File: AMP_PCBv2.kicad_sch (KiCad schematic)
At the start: 2 parts, among them U1 Teensy4.0, U2 Logo

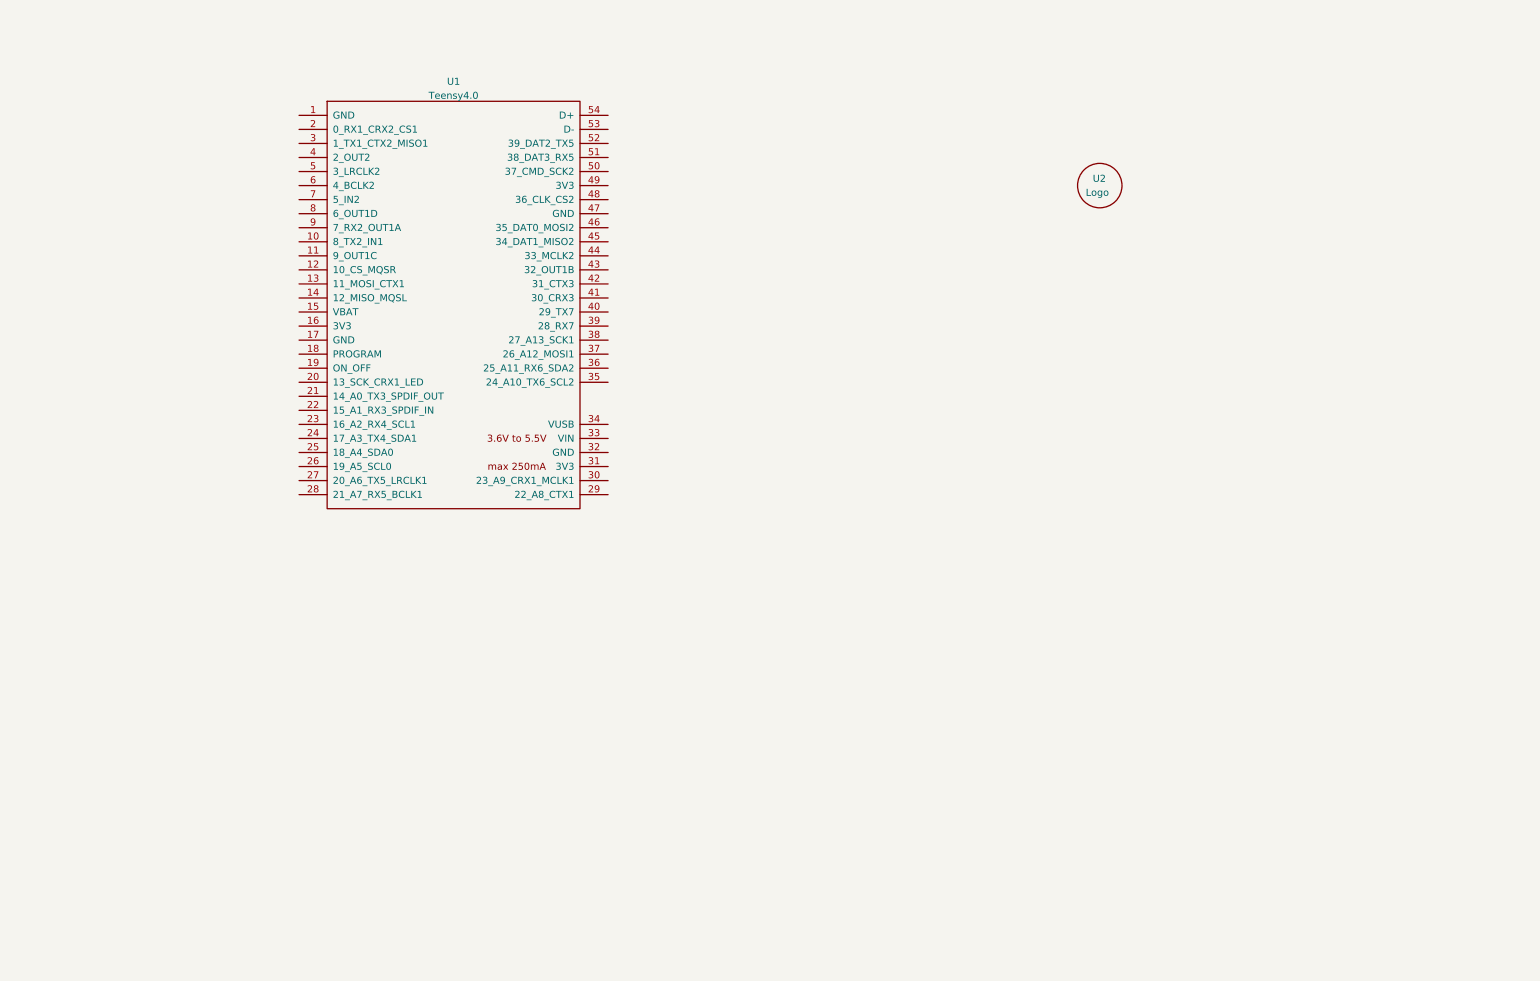
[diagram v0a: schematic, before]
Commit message: added bare bones schematic
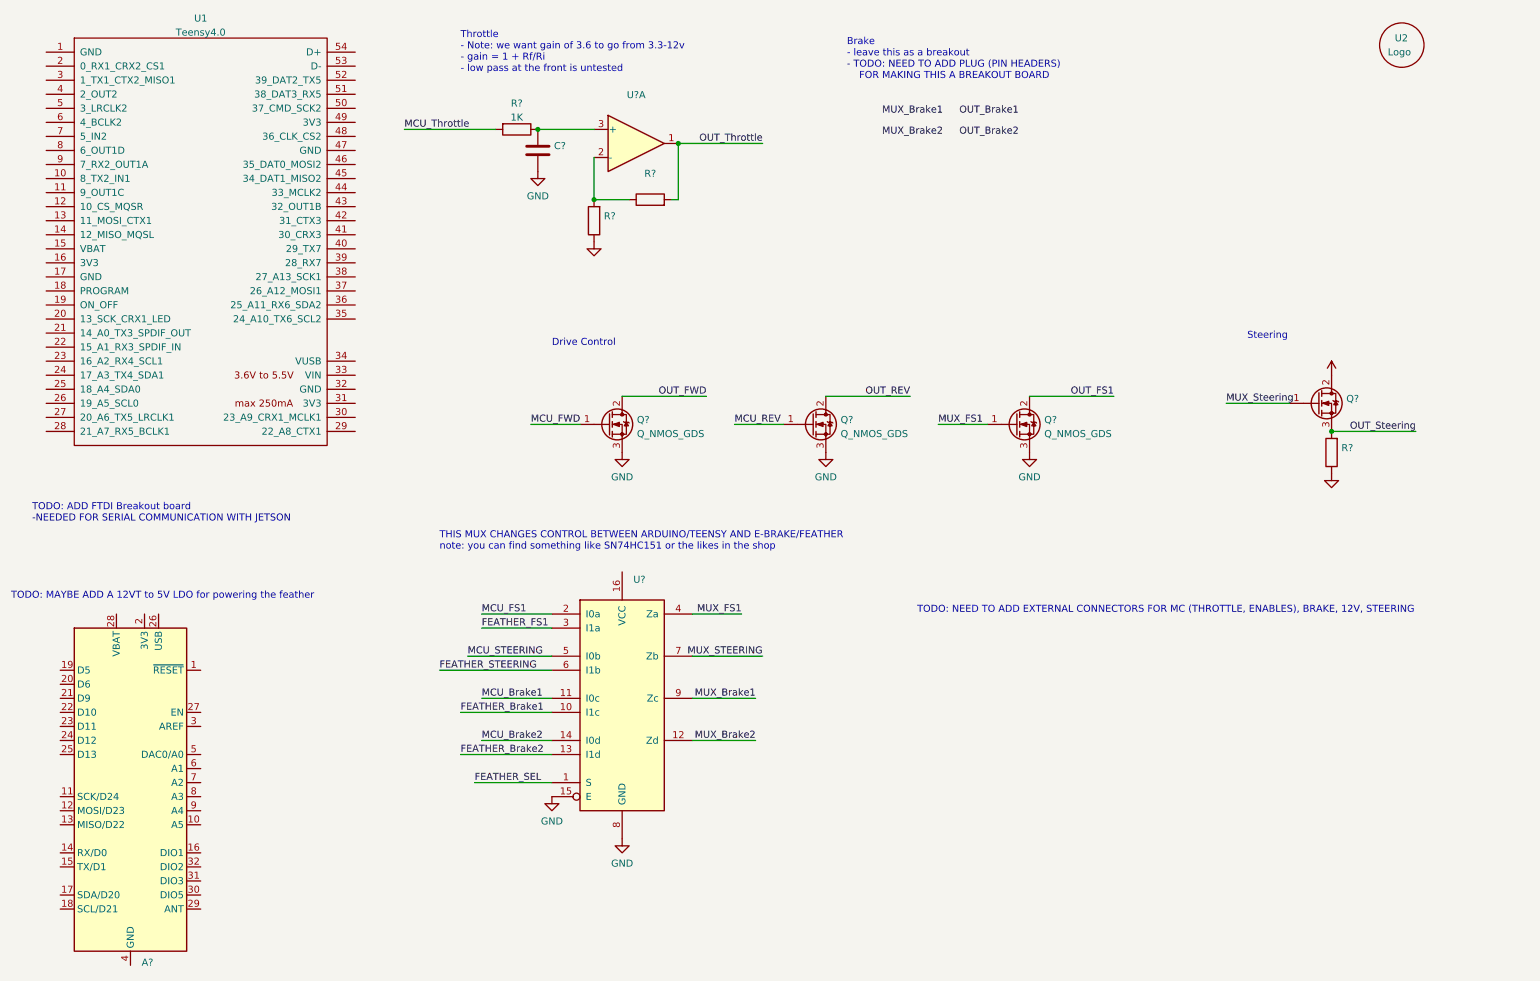
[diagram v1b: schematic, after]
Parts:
- added A?: (no value), symbol MCU_Module:Adafruit_Feather_M0_RFM9x_LoRa_Radio
- added C?: (no value), symbol Device:C
- added Q? (x3): Q_NMOS_GDS, symbol Device:Q_NMOS_GDS
- added Q?: (no value), symbol Device:Q_NMOS_GDS
- added R? (x3): (no value), symbol Device:R
- added R?: 1K, Resistor_THT:R_Axial_DIN0207_L6.3mm_D2.5mm_P10.16mm_Horizontal, symbol Device:R
- added U?: (no value), symbol Amplifier_Operational:TL084
- added U?: (no value), symbol 74xx:74LS157
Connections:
- new net: R?.1, R?.2, U?.2 (-)
- new net: C?.1, R?.1, U?.3 (+)
- new net +12V: Q?.2 (D)
- new net FEATHER_Brake1: U?.10 (I1c)
- new net FEATHER_Brake2: U?.13 (I1d)
- new net FEATHER_FS1: U?.3 (I1a)
- new net FEATHER_SEL: U?.1 (S)
- new net FEATHER_STEERING: U?.6 (I1b)
- new net GND: C?.2, Q?.3 (S), Q?.3 (S), Q?.3 (S), R?.1, R?.1, U?.15 (E), U?.8 (GND)
- new net MCU_Brake1: U?.11 (I0c)
- new net MCU_Brake2: U?.14 (I0d)
- new net MCU_FS1: U?.2 (I0a)
- new net MCU_FWD: Q?.1 (G)
- new net MCU_REV: Q?.1 (G)
- new net MCU_STEERING: U?.5 (I0b)
- new net MCU_Throttle: R?.2
- new net MUX_Brake1: U?.9 (Zc)
- new net MUX_Brake2: U?.12 (Zd)
- new net MUX_FS1: Q?.1 (G), U?.4 (Za)
- new net MUX_STEERING: U?.7 (Zb)
- new net MUX_Steering: Q?.1 (G)
- new net OUT_FS1: Q?.2 (D)
- new net OUT_FWD: Q?.2 (D)
- new net OUT_REV: Q?.2 (D)
- new net OUT_Steering: Q?.3 (S), R?.2
- new net OUT_Throttle: R?.2, U?.1
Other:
- note added: "Brake - leave this as a breakout - TODO: NEED TO ADD PLUG (PIN HEADERS) FOR MAKING THIS A BREAKOUT BOARD"
- note added: "Drive Control"
- note added: "Steering"
- note added: "THIS MUX CHANGES CONTROL BETWEEN ARDUINO/TEENSY AND E-BRAKE/FEATHER note: you can find something like SN74HC151 or the likes in the shop"
- note added: "TODO: ADD FTDI Breakout board -NEEDED FOR SERIAL COMMUNICATION WITH JETSON"
- note added: "TODO: MAYBE ADD A 12VT to 5V LDO for powering the feather"
- note added: "TODO: NEED TO ADD EXTERNAL CONNECTORS FOR MC (THROTTLE, ENABLES), BRAKE, 12V, STEERING"
- note added: "Throttle - Note: we want gain of 3.6 to go from 3.3-12v - gain = 1 + Rf/Ri - low pass at the front is untested"
- moved on the sheet: U1, U2

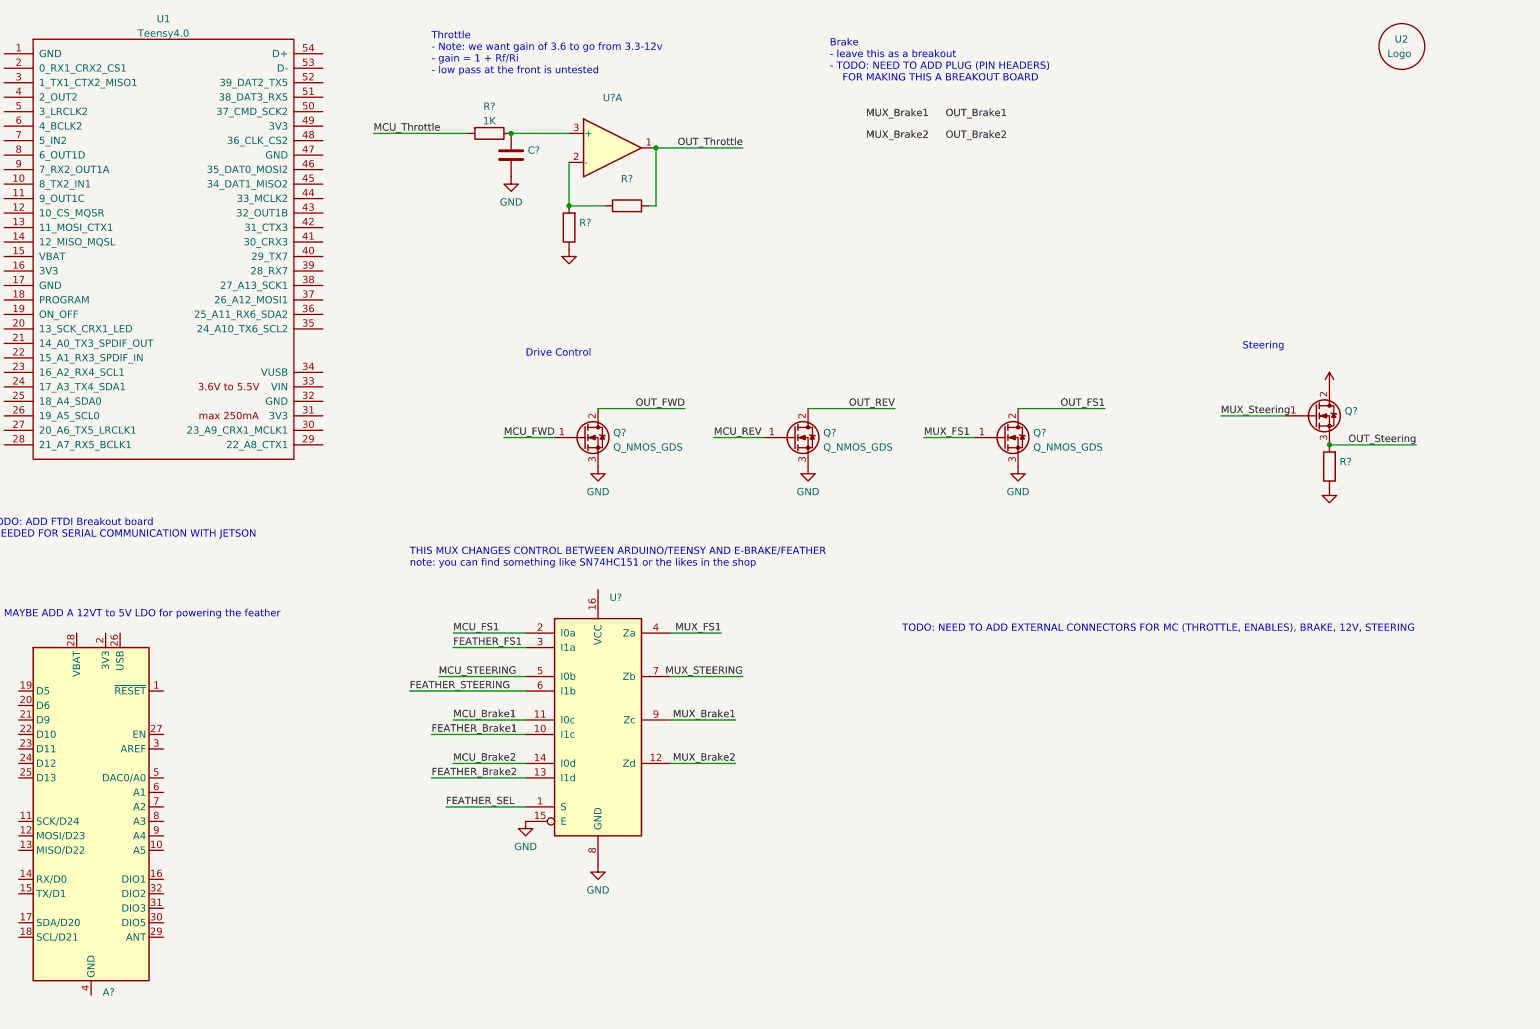
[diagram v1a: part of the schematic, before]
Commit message: Add MOSFET gate resistors, other misc cleanup
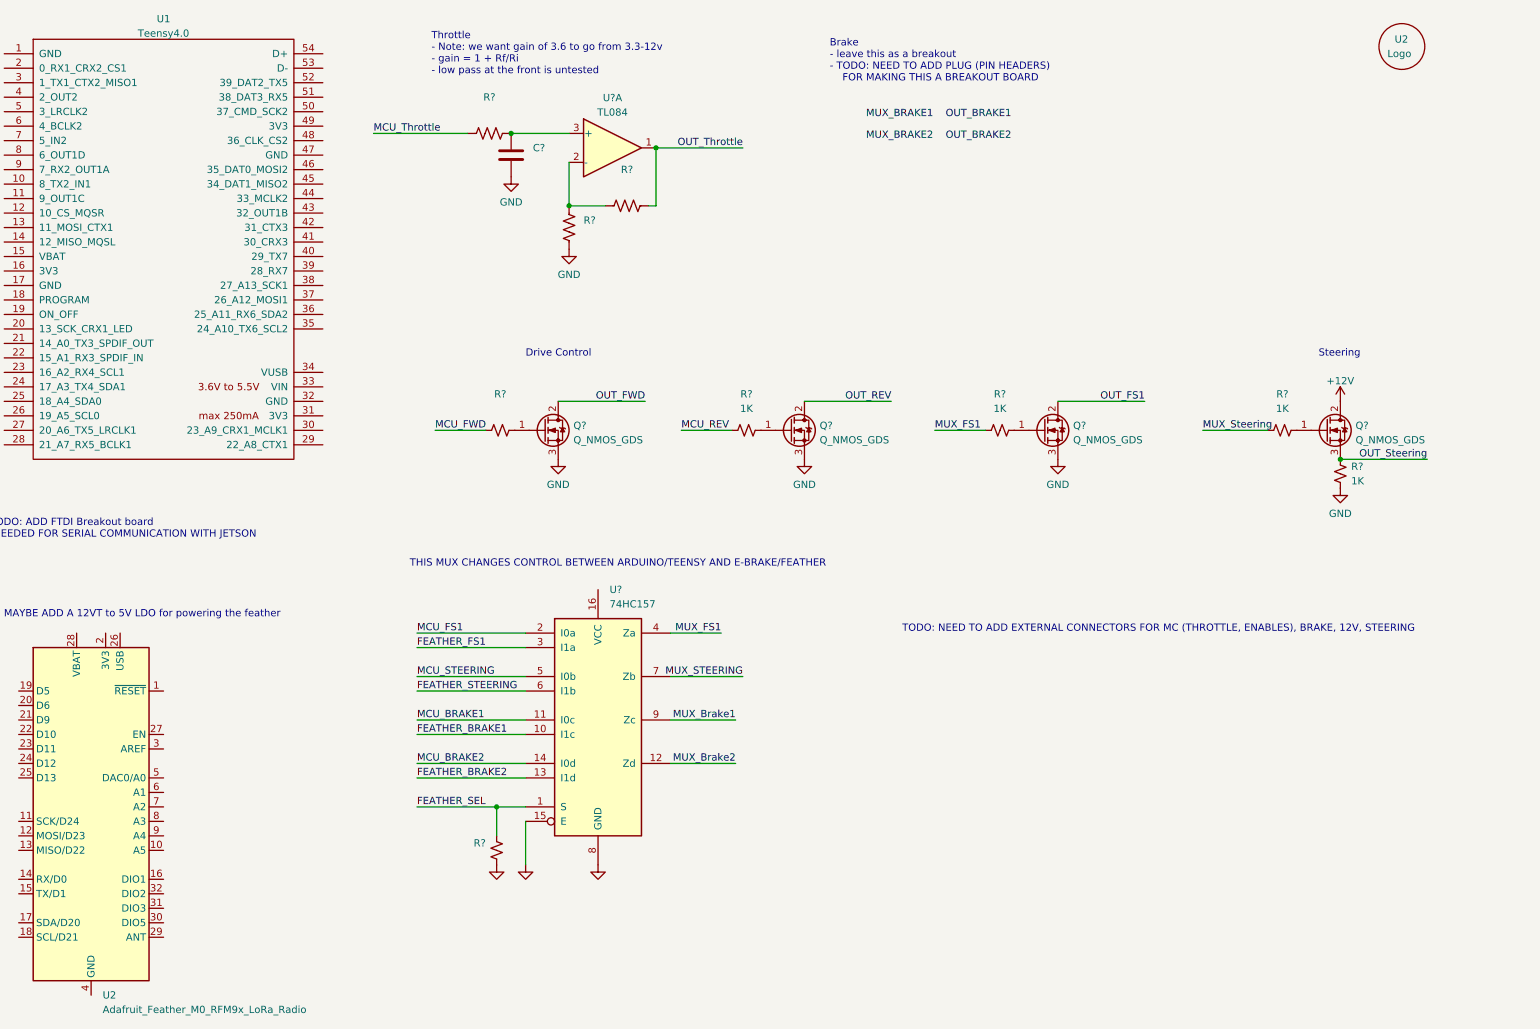
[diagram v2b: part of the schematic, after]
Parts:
- removed R? (x3): (no value), symbol Device:R
- removed R?: 1K, Resistor_THT:R_Axial_DIN0207_L6.3mm_D2.5mm_P10.16mm_Horizontal, symbol Device:R
- added R? (x2): (no value), symbol Device:R_Small_US
- added R? (x4): 1K, symbol Device:R_Small_US
- added R? (x3): (no value), symbol Device:R_US
- Q?: value (none) -> Q_NMOS_GDS
- U2: renamed from A?; value (none) -> Adafruit_Feather_M0_RFM9x_LoRa_Radio; footprint (none) -> Module:Adafruit_Feather_M0_RFM
- U?: value (none) -> TL084; footprint (none) -> Package_DIP:DIP-14_W7.62mm
- U?: value (none) -> 74HC157
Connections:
- net FEATHER_SEL: now also R?.1
- net GND: now also R?.1, R?.2, R?.2
- net MCU_FWD: now also R?.1; no longer Q?.1 (G)
- net MCU_REV: now also R?.1; no longer Q?.1 (G)
- net MCU_Throttle: now also R?.1
- net MUX_FS1: now also R?.1; no longer Q?.1 (G)
- net MUX_Steering: now also R?.1; no longer Q?.1 (G)
- net OUT_Steering: now also R?.2
- net OUT_Throttle: now also R?.2
- net at U?.2 (-): now also R?.1, R?.1
- net at C?.1, U?.3 (+): now also R?.2
- net FEATHER_Brake1 renamed FEATHER_BRAKE1
- net FEATHER_Brake2 renamed FEATHER_BRAKE2
- net MCU_Brake1 renamed MCU_BRAKE1
- net MCU_Brake2 renamed MCU_BRAKE2
- new net: Q?.1 (G), R?.2 (x4)
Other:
- note added: "THIS MUX CHANGES CONTROL BETWEEN ARDUINO/TEENSY AND E-BRAKE/FEATHER"
- note removed: "THIS MUX CHANGES CONTROL BETWEEN ARDUINO/TEENSY AND E-BRAKE/FEATHER note: you can find something like SN74HC151 or the likes in the shop"
- moved on the sheet: Q?
